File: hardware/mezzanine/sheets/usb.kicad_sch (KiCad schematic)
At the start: 19 parts

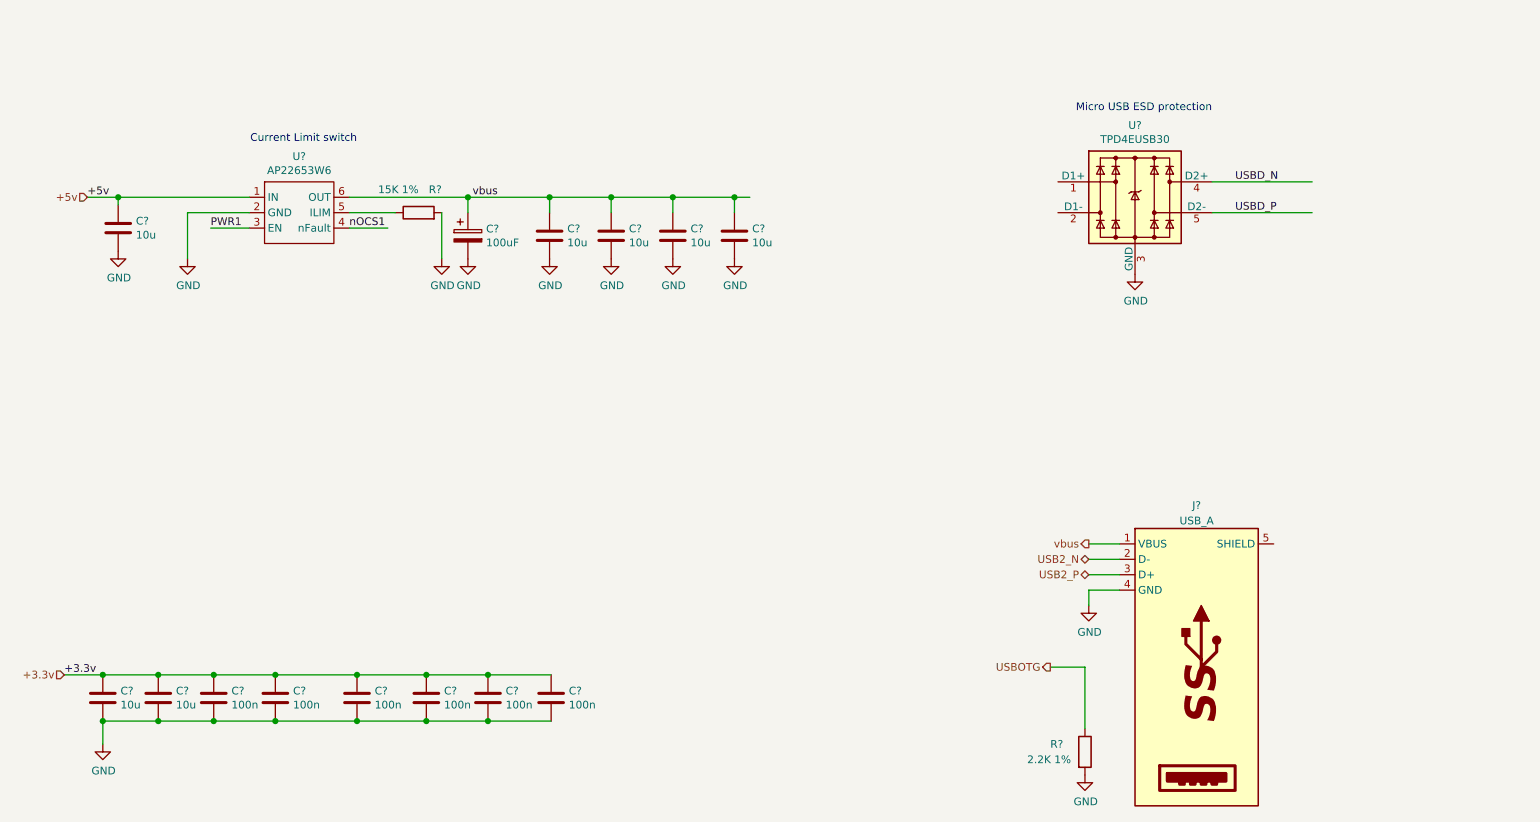
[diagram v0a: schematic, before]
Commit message: start routing mezzanine
making a progress capture before trying to cram a lot of signals onto just one hirose connector...
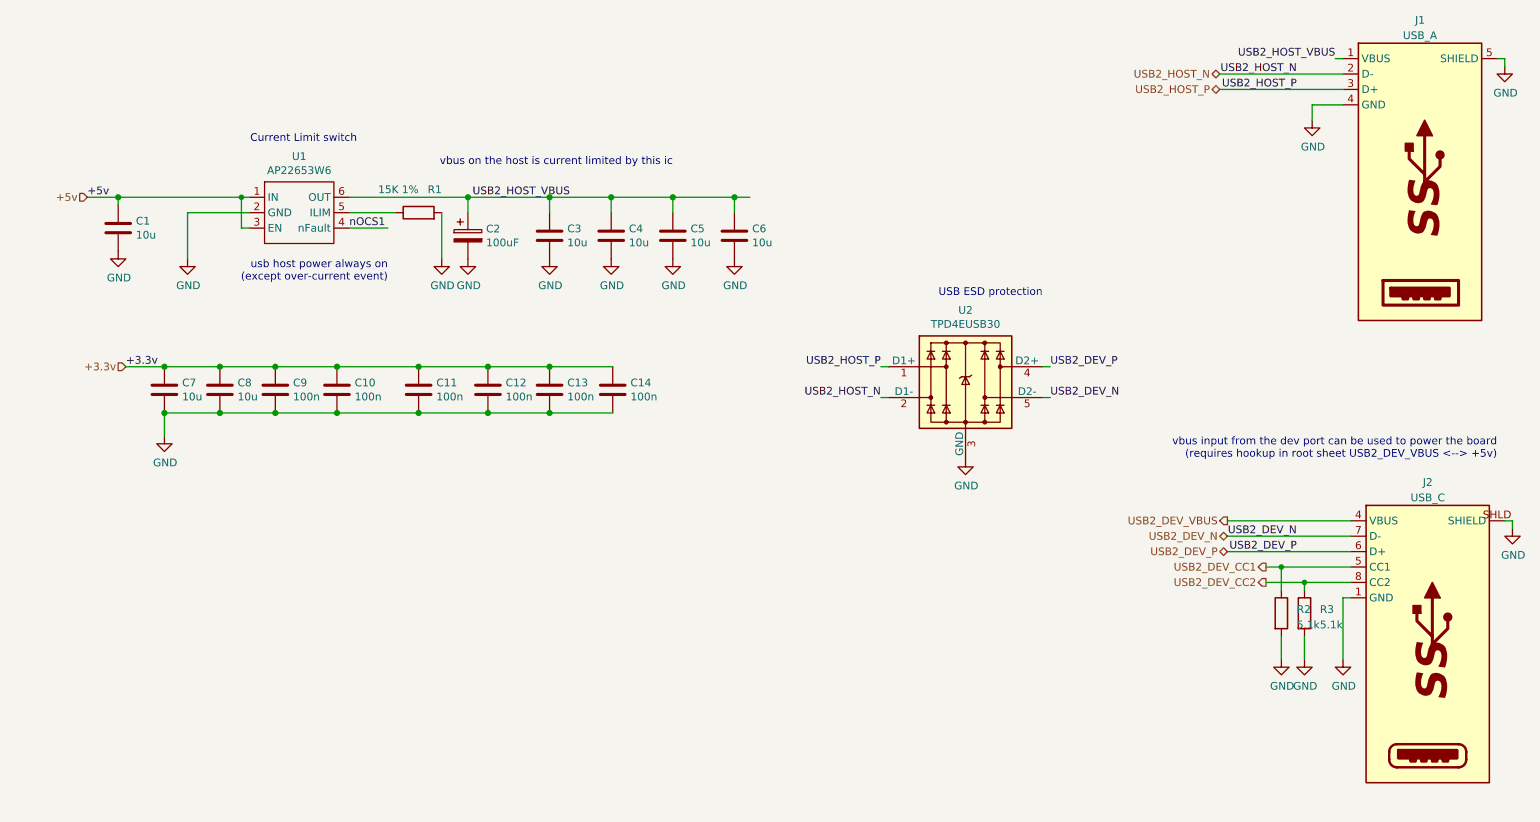
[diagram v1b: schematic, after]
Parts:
- removed R?: 2.2K 1%, Resistor_SMD:R_0402_1005Metric, symbol Device:R
- added J2: USB_C, cm4crypto:USB4105-GF-A, symbol CM4IO:USB_C
- added R2, R3: 5.1k, Resistor_SMD:R_0603_1608Metric, symbol Device:R
- J1: renamed from J?; footprint (none) -> cm4crypto:OnShore_USB-A1HSB6
- gave numbers to parts that had none: 17
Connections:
- net PWR1 is gone; now on net +5v: U1.3 (EN)
- net USB2_N is gone; now on net USB2_HOST_N: J1.2 (D-)
- net USB2_P is gone; now on net USB2_HOST_P: J1.3 (D+)
- net GND: now also J1.5 (SHIELD), J2.1 (GND), J2.12 (GND), J2.SHLD (SHIELD), R2.2, R3.2
- net USB2_HOST_P: now reaches U2.1 (D1+), U2.10
- net USB2_HOST_N: now reaches U2.2 (D1-), U2.9
- net USBD_N renamed USB2_DEV_P
- net USB2_DEV_P: now also J2.6 (D+)
- net USBD_P renamed USB2_DEV_N
- net USB2_DEV_N: now also J2.7 (D-)
- net vbus renamed USB2_HOST_VBUS
- new net USB2_DEV_CC1: J2.5 (CC1), R2.1
- new net USB2_DEV_CC2: J2.8 (CC2), R3.1
- new net VBUS: J2.4 (VBUS), J2.9 (VBUS)
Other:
- note added: "USB ESD protection"
- note added: "usb host power always on (except over-current event)"
- note added: "vbus input from the dev port can be used to power the board (requires hookup in root sheet USB2_DEV_VBUS <--> +5v)"
- note added: "vbus on the host is current limited by this ic"
- note removed: "Micro USB ESD protection"
- moved on the sheet: C10, C11, C12, C13, C14, C7, C8, C9, J1, U2

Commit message: finished mezzanine signal routing
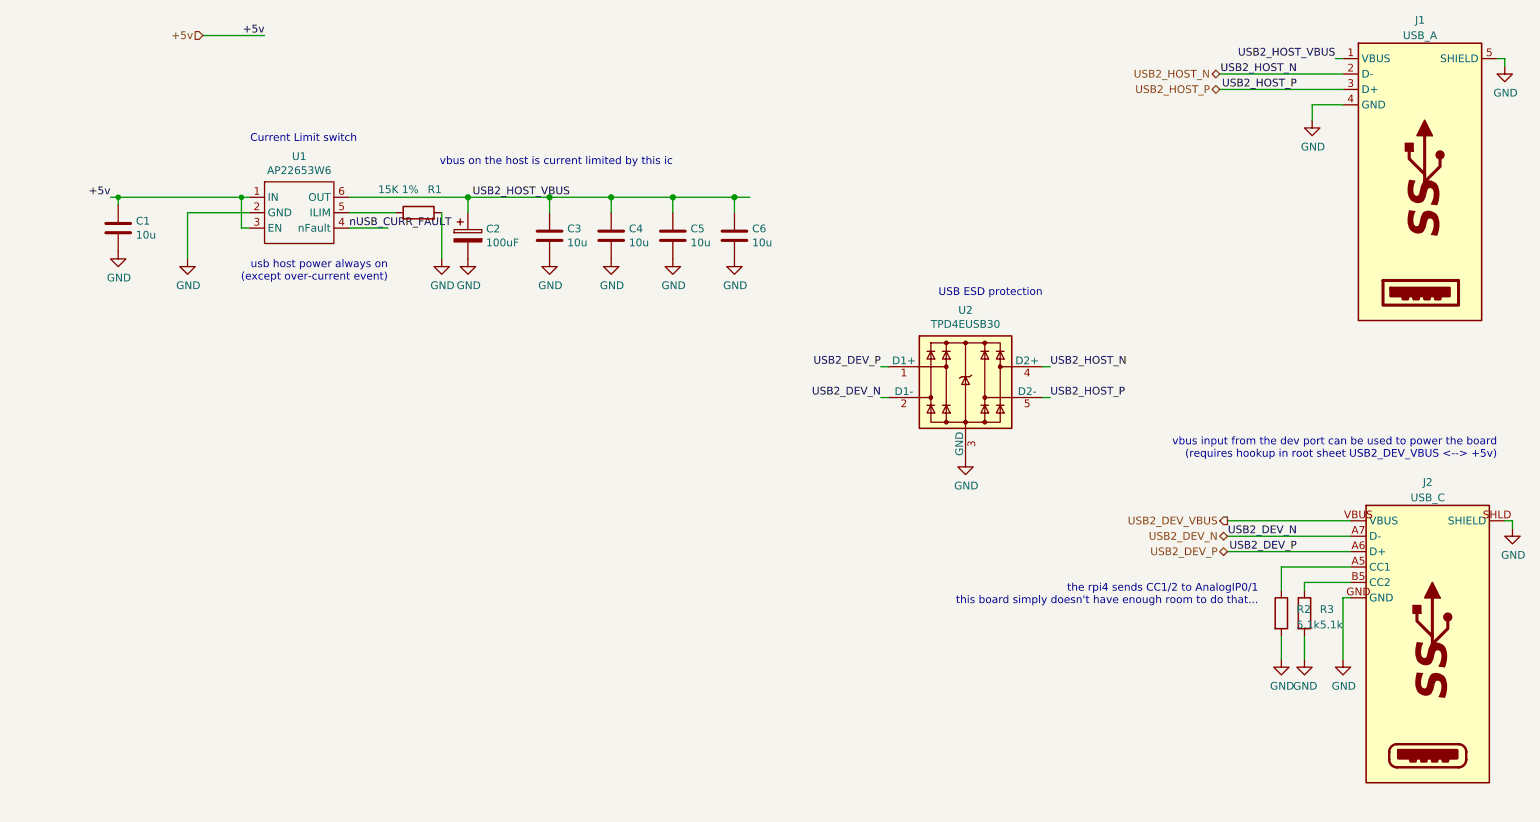
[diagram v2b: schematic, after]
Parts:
- removed C10, C11, C12, C13, C14, C9: 100n, Capacitor_SMD:C_0402_1005Metric, symbol Device:C
- removed C7, C8: 10u, Capacitor_SMD:C_0805_2012Metric, symbol Device:C
- removed J2: USB_C, cm4crypto:USB4105-GF-A, symbol CM4IO:USB_C
- added J2: USB_C, cm4crypto:USB4105-GF-A, symbol cm4crypto:USB_C
- C1, C3, C4, C5, C6: Field4 Digikey -> (none); Field5 490-14381-1-ND -> (none); Field6 GRM21BR71A106KA73L -> (none); Field7 Murata -> (none); Field8 111893011 -> (none); Part Description 10uF 10% 10V Ceramic Capacitor X7R 0805 (2012 Metric) -> (none)
- R1: footprint Resistor_SMD:R_0402_1005Metric -> Resistor_SMD:R_0805_2012Metric; Field4 Farnell -> (none); Field5 9239375 -> (none); Field6 MCR01MZPF1502 -> (none); Field7 Rohm -> (none); Field8 120891581 -> (none); Part Description Resistor 15K M1005 1% 63mW -> (none)
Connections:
- net GND: now also J2.GND, J2.SHLD (SHIELD)
- net USB2_DEV_N: now also U2.2 (D1-), U2.9, J2.A7 (D-), J2.B7 (D-); no longer U2.5 (D2-), U2.6
- net USB2_DEV_P: now also U2.1 (D1+), U2.10, J2.A6 (D+), J2.B6 (D+); no longer U2.4 (D2+), U2.7
- net USB2_HOST_N: now also U2.4 (D2+), U2.7; no longer U2.2 (D1-), U2.9
- net USB2_HOST_P: now also U2.5 (D2-), U2.6; no longer U2.1 (D1+), U2.10
- net VBUS: now also J2.VBUS
- net USB2_DEV_CC1: no longer names the net of R2.1
- net USB2_DEV_CC1: now also J2.A5 (CC1)
- net USB2_DEV_CC2: no longer names the net of R3.1
- net USB2_DEV_CC2: now also J2.B5 (CC2)
- net nOCS1 renamed nUSB_CURR_FAULT
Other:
- note added: "the rpi4 sends CC1/2 to AnalogIP0/1 this board simply doesn't have enough room to do that..."

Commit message: sheet refs relative, copied escalator pinout to lobby
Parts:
- renumbered C4 to C?, C3 to C?, C5 to C?, C6 to C?, C2 to C?, C1 to C?, J2 to J?, J1 to J?, R3 to R?, R1 to R?, R2 to R?, U2 to U?, U1 to U?
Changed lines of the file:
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@@
   (symbol (lib_id "power:GND") (at 46.99 58.42 0) (unit 1)
     (in_bom yes) (on_board yes)
-    (property "Reference" "#PWR033" (id 0) (at 46.99 64.77 0)
+    (property "Reference" "#PWR?" (id 0) (at 46.99 64.77 0)
       (effects (font (size 1.27 1.27)) hide)
     )
@@
   (symbol (lib_id "power:GND") (at 58.42 59.69 0) (unit 1)
     (in_bom yes) (on_board yes)
-    (property "Reference" "#PWR034" (id 0) (at 58.42 66.04 0)
+    (property "Reference" "#PWR?" (id 0) (at 58.42 66.04 0)
       (effects (font (size 1.27 1.27)) hide)
     )
@@
   (symbol (lib_id "power:GND") (at 100.33 59.69 0) (unit 1)
     (in_bom yes) (on_board yes)
-    (property "Reference" "#PWR035" (id 0) (at 100.33 66.04 0)
+    (property "Reference" "#PWR?" (id 0) (at 100.33 66.04 0)
       (effects (font (size 1.27 1.27)) hide)
     )
@@
   (symbol (lib_id "power:GND") (at 104.648 59.69 0) (unit 1)
     (in_bom yes) (on_board yes)
-    (property "Reference" "#PWR036" (id 0) (at 104.648 66.04 0)
+    (property "Reference" "#PWR?" (id 0) (at 104.648 66.04 0)
       (effects (font (size 1.27 1.27)) hide)
     )
@@
   (symbol (lib_id "power:GND") (at 118.11 59.69 0) (unit 1)
     (in_bom yes) (on_board yes)
-    (property "Reference" "#PWR037" (id 0) (at 118.11 66.04 0)
+    (property "Reference" "#PWR?" (id 0) (at 118.11 66.04 0)
       (effects (font (size 1.27 1.27)) hide)
     )
@@
   (symbol (lib_id "power:GND") (at 128.27 59.69 0) (unit 1)
     (in_bom yes) (on_board yes)
-    (property "Reference" "#PWR038" (id 0) (at 128.27 66.04 0)
+    (property "Reference" "#PWR?" (id 0) (at 128.27 66.04 0)
       (effects (font (size 1.27 1.27)) hide)
     )
@@
   (symbol (lib_id "power:GND") (at 138.43 59.69 0) (unit 1)
     (in_bom yes) (on_board yes)
-    (property "Reference" "#PWR039" (id 0) (at 138.43 66.04 0)
+    (property "Reference" "#PWR?" (id 0) (at 138.43 66.04 0)
       (effects (font (size 1.27 1.27)) hide)
     )
@@
   (symbol (lib_id "power:GND") (at 148.59 59.69 0) (unit 1)
     (in_bom yes) (on_board yes)
-    (property "Reference" "#PWR040" (id 0) (at 148.59 66.04 0)
+    (property "Reference" "#PWR?" (id 0) (at 148.59 66.04 0)
       (effects (font (size 1.27 1.27)) hide)
     )
@@
   (symbol (lib_id "power:GND") (at 186.69 92.71 0) (unit 1)
     (in_bom yes) (on_board yes)
-    (property "Reference" "#PWR041" (id 0) (at 186.69 99.06 0)
+    (property "Reference" "#PWR?" (id 0) (at 186.69 99.06 0)
       (effects (font (size 1.27 1.27)) hide)
     )
@@
   (symbol (lib_id "power:GND") (at 238.76 125.73 0) (unit 1)
     (in_bom yes) (on_board yes)
-    (property "Reference" "#PWR043" (id 0) (at 238.76 132.08 0)
+    (property "Reference" "#PWR?" (id 0) (at 238.76 132.08 0)
       (effects (font (size 1.27 1.27)) hide)
     )
@@
   (symbol (lib_id "power:GND") (at 242.57 125.73 0) (unit 1)
     (in_bom yes) (on_board yes)
-    (property "Reference" "#PWR044" (id 0) (at 242.57 132.08 0)
+    (property "Reference" "#PWR?" (id 0) (at 242.57 132.08 0)
       (effects (font (size 1.27 1.27)) hide)
     )
@@
   (symbol (lib_id "power:GND") (at 243.84 36.83 0) (unit 1)
     (in_bom yes) (on_board yes)
-    (property "Reference" "#PWR032" (id 0) (at 243.84 43.18 0)
+    (property "Reference" "#PWR?" (id 0) (at 243.84 43.18 0)
       (effects (font (size 1.27 1.27)) hide)
     )
@@
   (symbol (lib_id "power:GND") (at 248.92 125.73 0) (unit 1)
     (in_bom yes) (on_board yes)
-    (property "Reference" "#PWR045" (id 0) (at 248.92 132.08 0)
+    (property "Reference" "#PWR?" (id 0) (at 248.92 132.08 0)
       (effects (font (size 1.27 1.27)) hide)
     )
@@
   (symbol (lib_id "power:GND") (at 275.59 27.94 0) (unit 1)
     (in_bom yes) (on_board yes)
-    (property "Reference" "#PWR031" (id 0) (at 275.59 34.29 0)
+    (property "Reference" "#PWR?" (id 0) (at 275.59 34.29 0)
       (effects (font (size 1.27 1.27)) hide)
     )
@@
   (symbol (lib_id "power:GND") (at 276.86 104.14 0) (unit 1)
     (in_bom yes) (on_board yes)
-    (property "Reference" "#PWR042" (id 0) (at 276.86 110.49 0)
+    (property "Reference" "#PWR?" (id 0) (at 276.86 110.49 0)
       (effects (font (size 1.27 1.27)) hide)
     )
@@
   (symbol (lib_id "Device:R") (at 96.52 52.07 90) (unit 1)
     (in_bom yes) (on_board yes)
-    (property "Reference" "R1" (id 0) (at 100.33 48.26 90)
+    (property "Reference" "R?" (id 0) (at 100.33 48.26 90)
       (effects (font (size 1.27 1.27)) (justify left))
     )
@@
   (symbol (lib_id "Device:R") (at 238.76 118.11 0) (unit 1)
     (in_bom yes) (on_board yes) (fields_autoplaced)
-    (property "Reference" "R2" (id 0) (at 241.3 117.4749 0)
+    (property "Reference" "R?" (id 0) (at 241.3 117.4749 0)
       (effects (font (size 1.27 1.27)) (justify left))
     )
@@
   (symbol (lib_id "Device:R") (at 242.57 118.11 0) (unit 1)
     (in_bom yes) (on_board yes) (fields_autoplaced)
-    (property "Reference" "R3" (id 0) (at 245.11 117.4749 0)
+    (property "Reference" "R?" (id 0) (at 245.11 117.4749 0)
       (effects (font (size 1.27 1.27)) (justify left))
     )
@@
   (symbol (lib_id "Device:C") (at 46.99 54.61 0) (unit 1)
     (in_bom yes) (on_board yes)
-    (property "Reference" "C1" (id 0) (at 49.911 53.4416 0)
+    (property "Reference" "C?" (id 0) (at 49.911 53.4416 0)
       (effects (font (size 1.27 1.27)) (justify left))
     )
@@
   (symbol (lib_id "Device:CP") (at 104.648 55.88 0) (unit 1)
     (in_bom yes) (on_board yes)
-    (property "Reference" "C2" (id 0) (at 107.6452 54.737 0)
+    (property "Reference" "C?" (id 0) (at 107.6452 54.737 0)
       (effects (font (size 1.27 1.27)) (justify left))
     )
@@
   (symbol (lib_id "Device:C") (at 118.11 55.88 0) (unit 1)
     (in_bom yes) (on_board yes)
-    (property "Reference" "C3" (id 0) (at 121.031 54.7116 0)
+    (property "Reference" "C?" (id 0) (at 121.031 54.7116 0)
       (effects (font (size 1.27 1.27)) (justify left))
     )
@@
   (symbol (lib_id "Device:C") (at 128.27 55.88 0) (unit 1)
     (in_bom yes) (on_board yes)
-    (property "Reference" "C4" (id 0) (at 131.191 54.7116 0)
+    (property "Reference" "C?" (id 0) (at 131.191 54.7116 0)
       (effects (font (size 1.27 1.27)) (justify left))
     )
@@
   (symbol (lib_id "Device:C") (at 138.43 55.88 0) (unit 1)
     (in_bom yes) (on_board yes)
-    (property "Reference" "C5" (id 0) (at 141.351 54.7116 0)
+    (property "Reference" "C?" (id 0) (at 141.351 54.7116 0)
       (effects (font (size 1.27 1.27)) (justify left))
     )
@@
   (symbol (lib_id "Device:C") (at 148.59 55.88 0) (unit 1)
     (in_bom yes) (on_board yes)
-    (property "Reference" "C6" (id 0) (at 151.511 54.7116 0)
+    (property "Reference" "C?" (id 0) (at 151.511 54.7116 0)
       (effects (font (size 1.27 1.27)) (justify left))
     )
@@
   (symbol (lib_id "CM4IO:AP2553W6") (at 77.47 52.07 0) (unit 1)
     (in_bom yes) (on_board yes)
-    (property "Reference" "U1" (id 0) (at 76.835 42.799 0))
+    (property "Reference" "U?" (id 0) (at 76.835 42.799 0))
     (property "Value" "AP22653W6" (id 1) (at 76.835 45.1104 0))
     (property "Footprint" "Package_TO_SOT_SMD:SOT-23-6" (id 2) (at 81.28 58.42 0)
@@
   (symbol (lib_id "CM4IO:TPD4EUSB30") (at 186.69 80.01 0) (unit 1)
     (in_bom yes) (on_board yes)
-    (property "Reference" "U2" (id 0) (at 186.69 68.1482 0))
+    (property "Reference" "U?" (id 0) (at 186.69 68.1482 0))
     (property "Value" "TPD4EUSB30" (id 1) (at 186.69 70.4596 0))
     (property "Footprint" "Package_SON:USON-10_2.5x1.0mm_P0.5mm" (id 2) (at 162.56 90.17 0)
@@
   (symbol (lib_id "CM4IO:USB_A") (at 262.89 50.8 0) (unit 1)
     (in_bom yes) (on_board yes) (fields_autoplaced)
-    (property "Reference" "J1" (id 0) (at 261.62 20.32 0))
+    (property "Reference" "J?" (id 0) (at 261.62 20.32 0))
     (property "Value" "USB_A" (id 1) (at 261.62 22.86 0))
     (property "Footprint" "cm4crypto:OnShore_USB-A1HSB6" (id 2) (at 264.16 30.48 0)
@@
   (symbol (lib_id "cm4crypto:USB_C") (at 264.16 127 0) (unit 1)
     (in_bom yes) (on_board yes) (fields_autoplaced)
-    (property "Reference" "J2" (id 0) (at 262.89 96.52 0))
+    (property "Reference" "J?" (id 0) (at 262.89 96.52 0))
     (property "Value" "USB_C" (id 1) (at 262.89 99.06 0))
     (property "Footprint" "cm4crypto:USB4105-GF-A" (id 2) (at 265.43 106.68 0)
